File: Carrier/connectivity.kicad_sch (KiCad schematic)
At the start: 18 parts, among them U4 ESP32-C6-WROOM-1

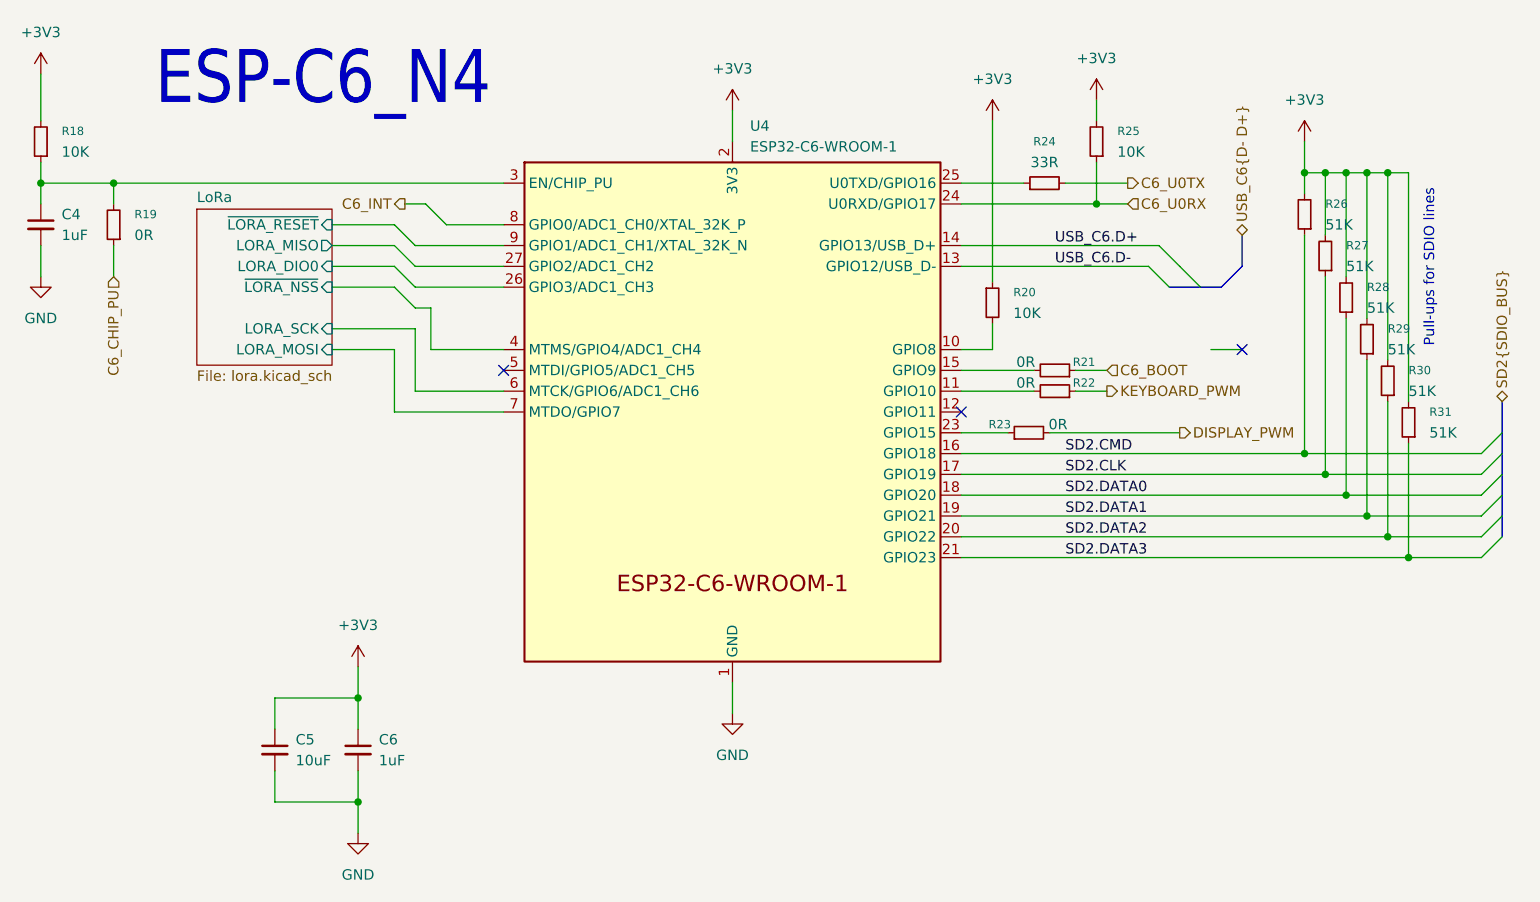
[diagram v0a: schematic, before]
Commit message: fix: sync schematic prot3 and v2.5
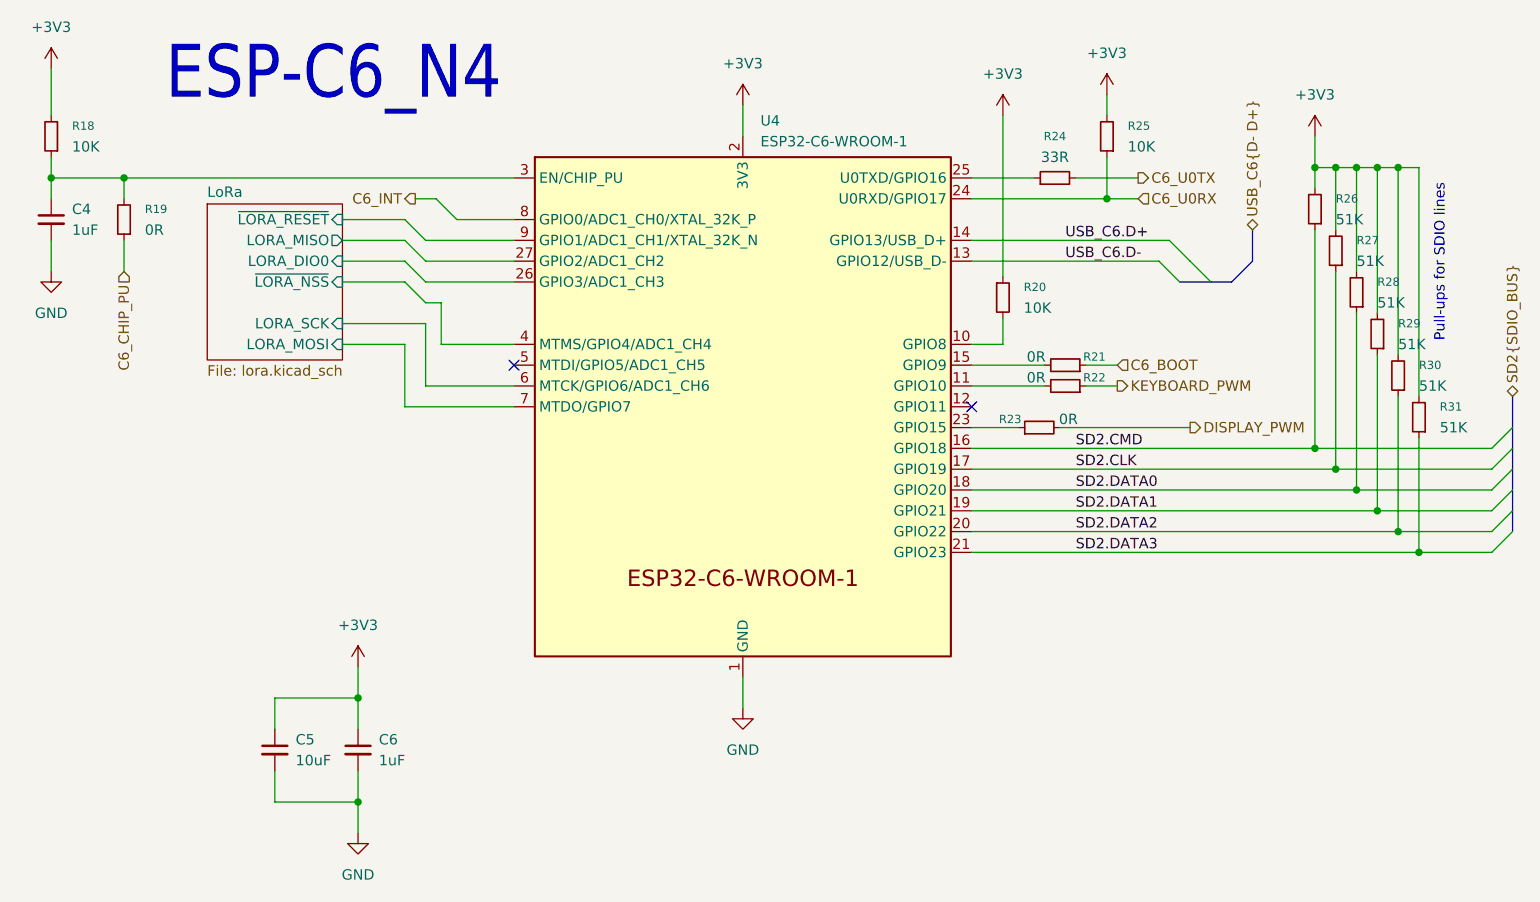
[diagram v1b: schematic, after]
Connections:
- no-connect marks 3 -> 2
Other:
- moved on the sheet: C4, R18, R19, R20, R21, R22, R23, R24, R25, R26, R27, R28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

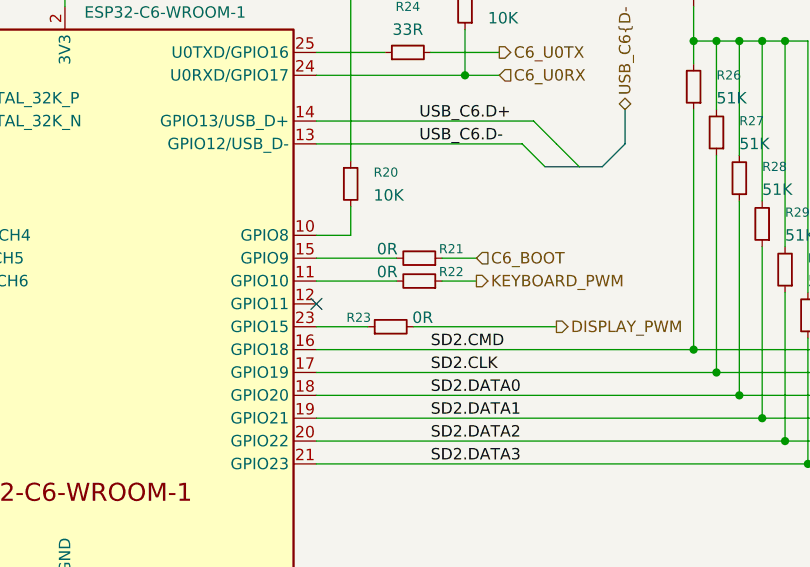
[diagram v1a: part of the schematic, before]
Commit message: Resistor value update c6
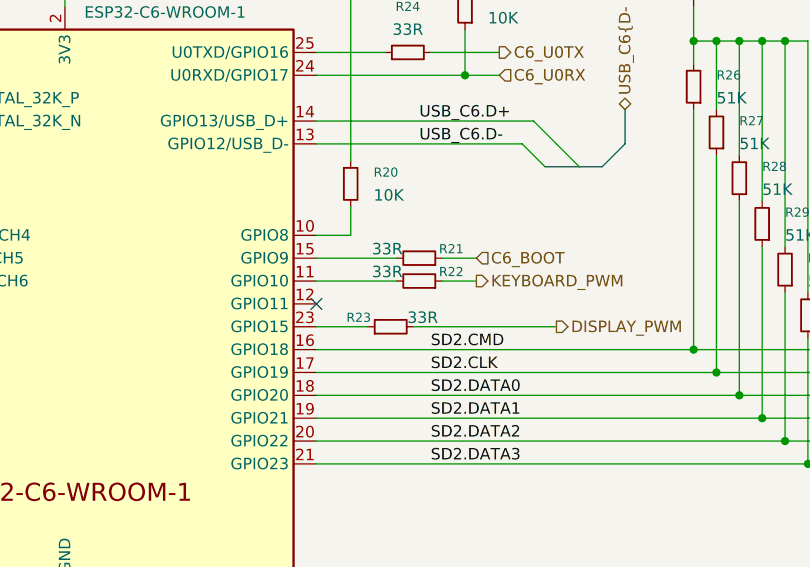
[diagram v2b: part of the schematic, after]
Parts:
- R21, R22, R23: value 0R -> 33R
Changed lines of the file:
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@@
 			)
 		)
-		(property "Value" "0R"
+		(property "Value" "33R"
 			(at 136.144 57.404 90)
 			(effects
@@
 			)
 		)
-		(property "Value" "0R"
+		(property "Value" "33R"
 			(at 140.081 62.484 90)
 			(effects
@@
 			)
 		)
-		(property "Value" "0R"
+		(property "Value" "33R"
 			(at 136.144 54.864 90)
 			(effects

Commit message: fix: add ordercodes for production files
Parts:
- R21: LCSC C17168 -> C25105
- R22: footprint Resistor_SMD:R_0603_1608Metric -> Resistor_SMD:R_0402_1005Metric; LCSC C17168 -> C25105
- R23: footprint Resistor_SMD:R_0603_1608Metric -> Resistor_SMD:R_0402_1005Metric; LCSC C15402 -> C25105
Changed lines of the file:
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@@
+			)
+		)
+		(property "Purchase-URL" ""
+			(at 172.72 41.91 0)
+			(effects
+				(font
+					(size 1.27 1.27)
+				)
+				(hide yes)
 			)
 		)
@@
 			)
 		)
+		(property "Purchase-URL" ""
+			(at 177.8 52.07 0)
+			(effects
+				(font
+					(size 1.27 1.27)
+				)
+				(hide yes)
+			)
+		)
 		(pin "1"
 		)
@@
 			)
 		)
+		(property "Purchase-URL" ""
+			(at 175.26 46.99 0)
+			(effects
+				(font
+					(size 1.27 1.27)
+				)
+				(hide yes)
+			)
+		)
 		(pin "1"
 		)
@@
 			)
 		)
-		(property "Footprint" "Resistor_SMD:R_0603_1608Metric"
+		(property "Footprint" "Resistor_SMD:R_0402_1005Metric"
 			(at 139.7 58.42 0)
 			(effects
@@
 			)
 		)
-		(property "LCSC" "C17168"
+		(property "LCSC" "C25105"
 			(at 139.7 58.42 0)
 			(effects
@@
 					(size 1.27 1.27)
 				)
+			)
+		)
+		(property "Purchase-URL" ""
+			(at 139.7 58.42 90)
+			(effects
+				(font
+					(size 1.27 1.27)
+				)
+				(hide yes)
 			)
 		)
@@
 			)
 		)
+		(property "Purchase-URL" ""
+			(at 182.88 62.23 0)
+			(effects
+				(font
+					(size 1.27 1.27)
+				)
+				(hide yes)
+			)
+		)
 		(pin "1"
 		)
@@
 			)
 		)
+		(property "Purchase-URL" ""
+			(at 132.08 47.625 0)
+			(effects
+				(font
+					(size 1.27 1.27)
+				)
+				(hide yes)
+			)
+		)
 		(pin "1"
 		)
@@
 			)
 		)
+		(property "Purchase-URL" ""
+			(at 15.875 27.94 0)
+			(effects
+				(font
+					(size 1.27 1.27)
+				)
+				(hide yes)
+			)
+		)
 		(pin "1"
 		)
@@
 			)
 		)
+		(property "Purchase-URL" ""
+			(at 100.33 60.96 0)
+			(effects
+				(font
+					(size 1.27 1.27)
+				)
+				(hide yes)
+			)
+		)
 		(pin "29"
 		)
@@
 			)
 		)
+		(property "Purchase-URL" ""
+			(at 24.765 38.1 0)
+			(effects
+				(font
+					(size 1.27 1.27)
+				)
+				(hide yes)
+			)
+		)
 		(pin "1"
 		)
@@
 			)
 		)
+		(property "Purchase-URL" ""
+			(at 53.34 102.87 0)
+			(effects
+				(font
+					(size 1.27 1.27)
+				)
+				(hide yes)
+			)
+		)
 		(pin "2"
 		)
@@
 			)
 		)
-		(property "Footprint" "Resistor_SMD:R_0603_1608Metric"
+		(property "Footprint" "Resistor_SMD:R_0402_1005Metric"
 			(at 136.525 63.5 0)
 			(effects
@@
 			)
 		)
-		(property "LCSC" "C15402"
+		(property "LCSC" "C25105"
 			(at 136.525 63.5 0)
 			(effects
@@
 					(size 1.27 1.27)
 				)
+			)
+		)
+		(property "Purchase-URL" ""
+			(at 136.525 63.5 90)
+			(effects
+				(font
+					(size 1.27 1.27)
+				)
+				(hide yes)
 			)
 		)
@@
 			)
 		)
+		(property "Purchase-URL" ""
+			(at 144.78 27.94 0)
+			(effects
+				(font
+					(size 1.27 1.27)
+				)
+				(hide yes)
+			)
+		)
 		(pin "1"
 		)
@@
 			)
 		)
+		(property "Purchase-URL" ""
+			(at 170.18 36.83 0)
+			(effects
+				(font
+					(size 1.27 1.27)
+				)
+				(hide yes)
+			)
+		)
 		(pin "1"
 		)
@@
 			)
 		)
+		(property "Purchase-URL" ""
+			(at 138.43 33.02 90)
+			(effects
+				(font
+					(size 1.27 1.27)
+				)
+				(hide yes)
+			)
+		)
 		(pin "1"
 		)
@@
 			)
 		)
+		(property "Purchase-URL" ""
+			(at 180.34 57.15 0)
+			(effects
+				(font
+					(size 1.27 1.27)
+				)
+				(hide yes)
+			)
+		)
 		(pin "1"
 		)
@@
 			)
 		)
-		(property "LCSC" "C17168"
+		(property "LCSC" "C25105"
 			(at 139.7 55.88 0)
 			(effects
@@
 					(size 1.27 1.27)
 				)
+			)
+		)
+		(property "Purchase-URL" ""
+			(at 139.7 55.88 90)
+			(effects
+				(font
+					(size 1.27 1.27)
+				)
+				(hide yes)
 			)
 		)
@@
 			)
 		)
+		(property "Purchase-URL" ""
+			(at 43.18 102.87 0)
+			(effects
+				(font
+					(size 1.27 1.27)
+				)
+				(hide yes)
+			)
+		)
 		(pin "2"
 		)
@@
 			)
 		)
+		(property "Purchase-URL" ""
+			(at 15.875 38.1 0)
+			(effects
+				(font
+					(size 1.27 1.27)
+				)
+				(hide yes)
+			)
+		)
